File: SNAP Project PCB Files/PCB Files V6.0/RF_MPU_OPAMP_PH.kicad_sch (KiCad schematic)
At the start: 52 parts, among them IC2 STM32WB35CCU7A, Q4 SFH 310, SW2 SW_Push, SW3 SW_Push, SW4 SW_Push, SW5 SW_Push, U5 LT1077CN8, U6 LT1077CN8, U7 LT1077CN8, Y1 XRCGB32M000F0Z00R0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

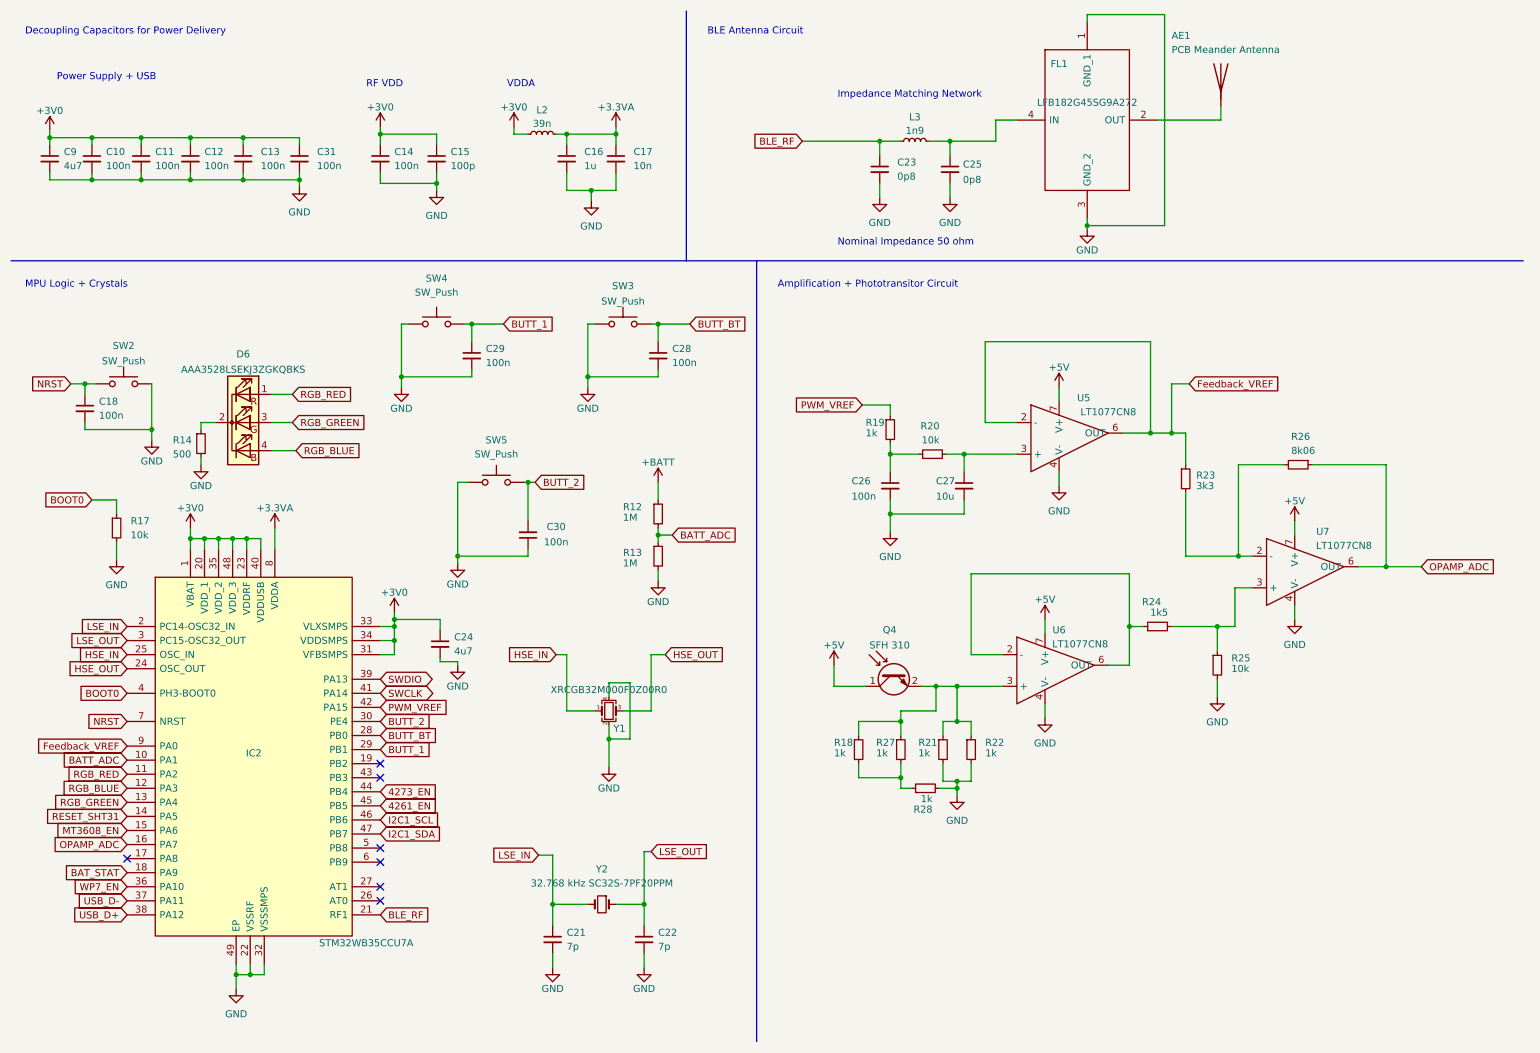
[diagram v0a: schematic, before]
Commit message: Updated Connectors, LEDs, filter and STM I/O
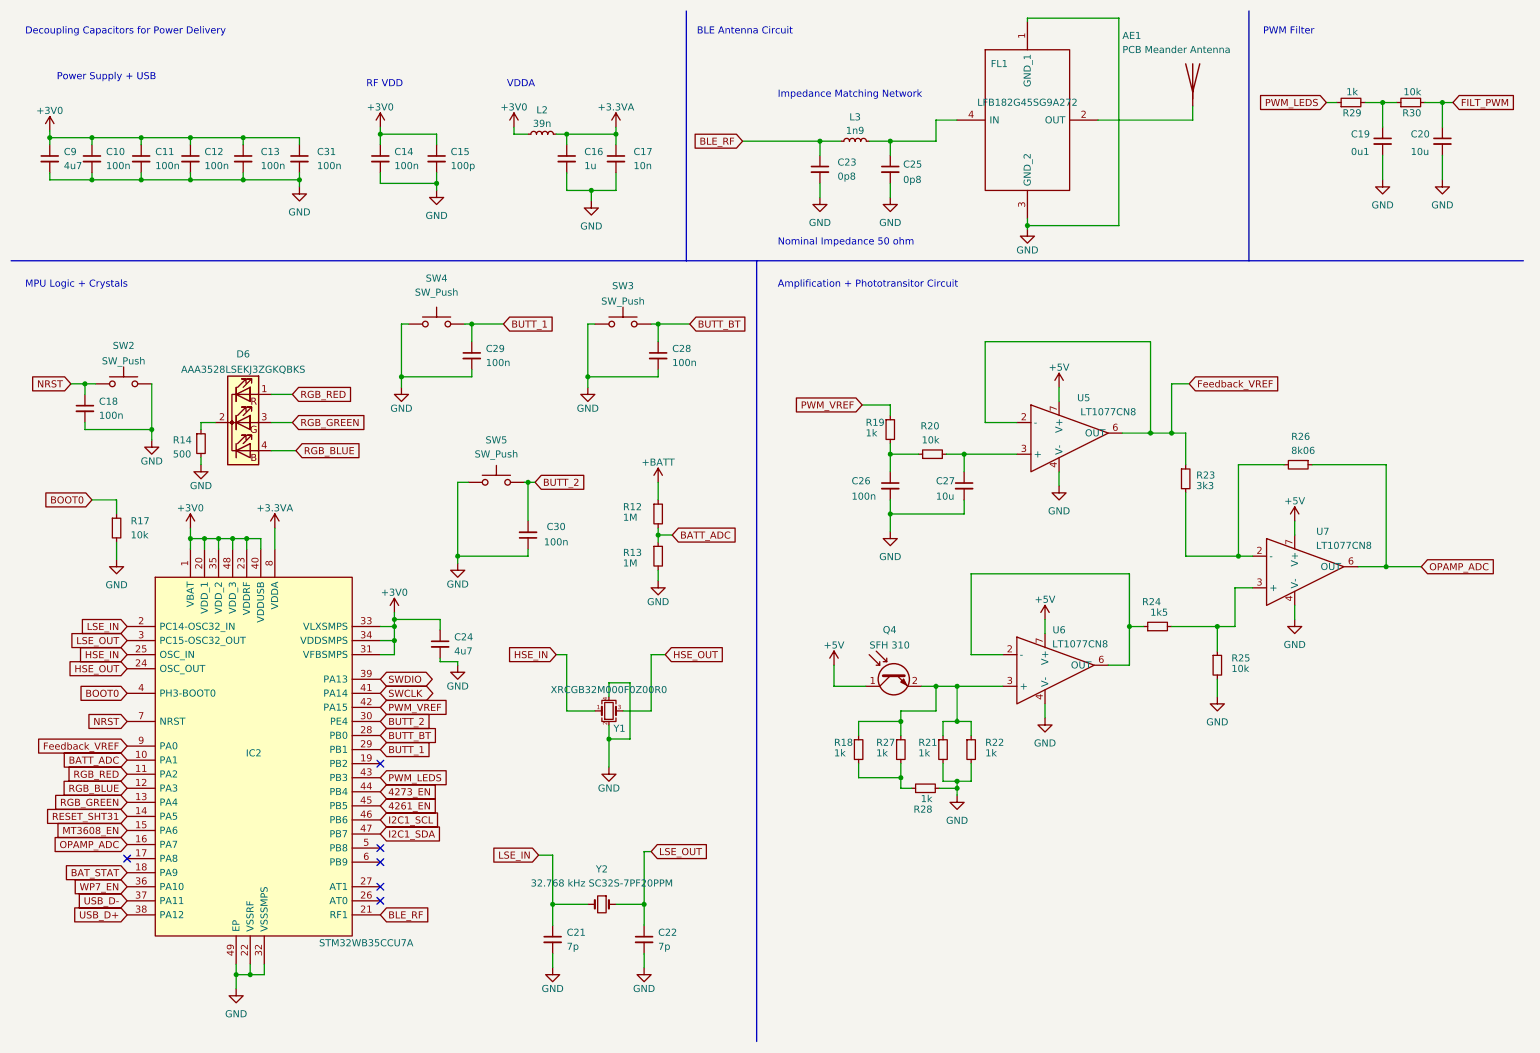
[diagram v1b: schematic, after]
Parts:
- added C19: 0u1, Capacitor_SMD:C_0402_1005Metric, symbol Device:C_Small
- added C20: 10u, Capacitor_SMD:C_0402_1005Metric, symbol Device:C_Small
- added R29: 1k, Resistor_SMD:R_0805_2012Metric, symbol Device:R_Small
- added R30: 10k, Resistor_SMD:R_0805_2012Metric, symbol Device:R_Small
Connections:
- net GND: now also C19.2, C20.2
- net PWM_LEDS: now reaches IC2.43 (PB3)
- net PWM_LEDS: now also R29.1
- new net: C19.1, R29.2, R30.1
- new net FILT_PWM: C20.1, R30.2
- no-connect marks 7 -> 6
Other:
- note added: "PWM Filter"
- moved on the sheet: AE1, C23, C25, FL1, L3

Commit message: Final Commit V 6.1
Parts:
- R23: value 3k3 -> 2k2
- R24: value 1k5 -> 4k7
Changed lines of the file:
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@@
       (effects (font (size 1.27 1.27)) (justify left))
     )
-    (property "Value" "3k3" (id 1) (at 225.425 97.79 0)
+    (property "Value" "2k2" (id 1) (at 225.425 97.79 0)
       (effects (font (size 1.27 1.27)) (justify left))
     )
@@
   (symbol (lib_id "Device:R_Small") (at 218.44 123.19 90) (unit 1)
     (in_bom yes) (on_board yes)
-    (property "Reference" "R24" (id 0) (at 219.075 118.745 90)
-      (effects (font (size 1.27 1.27)) (justify left))
-    )
-    (property "Value" "1k5" (id 1) (at 220.345 120.65 90)
-      (effects (font (size 1.27 1.27)) (justify left))
-    )
+    (property "Reference" "R24" (id 0) (at 220.345 118.745 90)
+      (effects (font (size 1.27 1.27)) (justify left))
+    )
+    (property "Value" "4k7" (id 1) (at 220.345 120.65 90)
+      (effects (font (size 1.27 1.27)) (justify left))
+    )
